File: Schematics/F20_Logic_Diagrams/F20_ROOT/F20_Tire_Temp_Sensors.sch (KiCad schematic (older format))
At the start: 6 parts

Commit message: 02/18/20 update
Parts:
- gave numbers to parts that had none: 6
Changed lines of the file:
@@
 $Descr A 11000 8500
 encoding utf-8
-Sheet 11 11
+Sheet 11 13
 Title "Tire Temperature Sensors"
 Date "2020-02-12"
@@
 $EndDescr
 $Comp
-L FSAE_Library:Tire_Temp_Sensor U?
+L FSAE_Library:Tire_Temp_Sensor U18
 U 1 1 5E3B80AD
 P 8500 1000
-F 0 "U?" H 9028 725 50  0000 L CNN
+F 0 "U18" H 9028 725 50  0000 L CNN
 F 1 "Tire_Temp_Sensor" H 8650 1050 50  0001 C CNN
 F 2 "" H 9000 1500 50  0001 C CNN
@@
 $EndComp
 $Comp
-L FSAE_Library:Tire_Temp_Sensor U?
+L FSAE_Library:Tire_Temp_Sensor U19
 U 1 1 5E3B9299
 P 8500 2000
-F 0 "U?" H 9028 1725 50  0000 L CNN
+F 0 "U19" H 9028 1725 50  0000 L CNN
 F 1 "Tire_Temp_Sensor" H 8650 2050 50  0001 C CNN
 F 2 "" H 9000 2500 50  0001 C CNN
@@
 $EndComp
 $Comp
-L FSAE_Library:Tire_Temp_Sensor U?
+L FSAE_Library:Tire_Temp_Sensor U20
 U 1 1 5E3BA080
 P 8500 3000
-F 0 "U?" H 9028 2725 50  0000 L CNN
+F 0 "U20" H 9028 2725 50  0000 L CNN
 F 1 "Tire_Temp_Sensor" H 8650 3050 50  0001 C CNN
 F 2 "" H 9000 3500 50  0001 C CNN
@@
 $EndComp
 $Comp
-L FSAE_Library:Tire_Temp_Sensor U?
+L FSAE_Library:Tire_Temp_Sensor U21
 U 1 1 5E3BAAB5
 P 8500 4000
-F 0 "U?" H 9028 3725 50  0000 L CNN
+F 0 "U21" H 9028 3725 50  0000 L CNN
 F 1 "Tire_Temp_Sensor" H 8650 4050 50  0001 C CNN
 F 2 "" H 9000 4500 50  0001 C CNN
@@
 RIM_LO_TIRE
 $Comp
-L FSAE_Library:Tire_Temp_Sensor U?
+L FSAE_Library:Tire_Temp_Sensor U22
 U 1 1 5E3CA66D
 P 8500 5000
-F 0 "U?" H 9028 4725 50  0000 L CNN
+F 0 "U22" H 9028 4725 50  0000 L CNN
 F 1 "Tire_Temp_Sensor" H 8650 5050 50  0001 C CNN
 F 2 "" H 9000 5500 50  0001 C CNN
@@
 RM
 $Comp
-L FSAE_Library:GND #PWR?
+L FSAE_Library:GND #PWR016
 U 1 1 5E3CA678
 P 4000 6950
-F 0 "#PWR?" H 4000 6750 50  0001 C CNN
+F 0 "#PWR016" H 4000 6750 50  0001 C CNN
 F 1 "GND" H 4004 6796 50  0000 C CNN
 F 2 "" H 4000 6900 50  0001 C CNN
@@
 RIM_+5V
 $Comp
-L FSAE_Library:Tire_Temp_Sensor U?
+L FSAE_Library:Tire_Temp_Sensor U23
 U 1 1 5E3CFAE2
 P 8500 6000
-F 0 "U?" H 9028 5725 50  0000 L CNN
+F 0 "U23" H 9028 5725 50  0000 L CNN
 F 1 "Tire_Temp_Sensor" H 8650 6050 50  0001 C CNN
 F 2 "" H 9000 6500 50  0001 C CNN

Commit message: 02/19/20 update
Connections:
- net RIM_LC_TIRE renamed LC_TIRE_TEMP
- net RIM_LI_TIRE renamed LI_TIRE_TEMP
- net RIM_LO_TIRE renamed LO_TIRE_TEMP
- net RIM_RI_TIRE renamed RI_TIRE_TEMP
- net RIM_RM_TIRE renamed RC_TIRE_TEMP
- net RM_RO_TIRE renamed RO_TIRE_TEMP
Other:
- note added: "LO: Left Outer\nLC: Left Center\nLI: Left Inner\nRO: Right Outer\nRC: Right Center\nRI: Right Inner\n\nAbout 2mA each\n18mA total"
- note removed: "LO: Left Outer\nLC: Left Center\nLI: Left Inner\nRO: Right Outer\nRC: Right Center\nRI: Right Inner"
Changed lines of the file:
@@
 $Descr A 11000 8500
 encoding utf-8
-Sheet 11 13
+Sheet 12 13
 Title "Tire Temperature Sensors"
 Date "2020-02-12"
@@
 Wire Wire Line
 	3500 2000 8500 2000
-Text GLabel 2500 1250 0    50   Input ~ 0
-RIM_LO_TIRE
 $Comp
 L FSAE_Library:Tire_Temp_Sensor U22
@@
 Wire Wire Line
 	3500 5000 8500 5000
-Text GLabel 2500 2250 0    50   Input ~ 0
-RIM_LC_TIRE
-Text GLabel 2500 3250 0    50   Input ~ 0
-RIM_LI_TIRE
-Text GLabel 2500 4250 0    50   Input ~ 0
-RIM_RI_TIRE
-Text GLabel 2500 5250 0    50   Input ~ 0
-RIM_RM_TIRE
-Text Notes 5550 7550 0    50   ~ 0
-LO: Left Outer\nLC: Left Center\nLI: Left Inner\nRO: Right Outer\nRC: Right Center\nRI: Right Inner
 Wire Notes Line
 	6275 7000 5500 7000
 Wire Notes Line
-	5500 7000 5500 7600
+	5500 7000 5500 7800
 Wire Notes Line
-	5500 7600 6275 7600
+	5500 7800 6275 7800
 Wire Wire Line
 	8500 6000 3500 6000
-Text GLabel 2500 6250 0    50   Input ~ 0
-RM_RO_TIRE
 Wire Wire Line
 	2500 1250 8500 1250
@@
 Wire Wire Line
 	2500 6250 8500 6250
+Text GLabel 2500 1250 0    50   Input ~ 0
+LO_TIRE_TEMP
+Text GLabel 2500 2250 0    50   Input ~ 0
+LC_TIRE_TEMP
+Text GLabel 2500 3250 0    50   Input ~ 0
+LI_TIRE_TEMP
+Text GLabel 2500 4250 0    50   Input ~ 0
+RI_TIRE_TEMP
+Text GLabel 2500 5250 0    50   Input ~ 0
+RC_TIRE_TEMP
+Text GLabel 2500 6250 0    50   Input ~ 0
+RO_TIRE_TEMP
+Text Notes 5550 7750 0    50   ~ 0
+LO: Left Outer\nLC: Left Center\nLI: Left Inner\nRO: Right Outer\nRC: Right Center\nRI: Right Inner\n\nAbout 2mA each\n18mA total
 $EndSCHEMATC

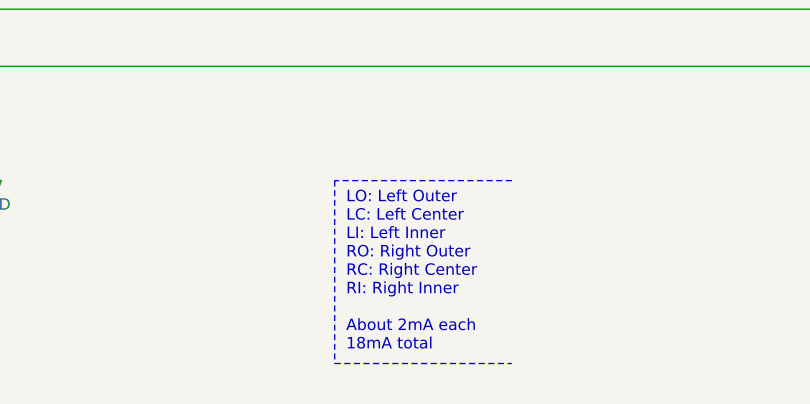
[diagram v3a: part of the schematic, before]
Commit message: Major powertrain update, added shifting schematic
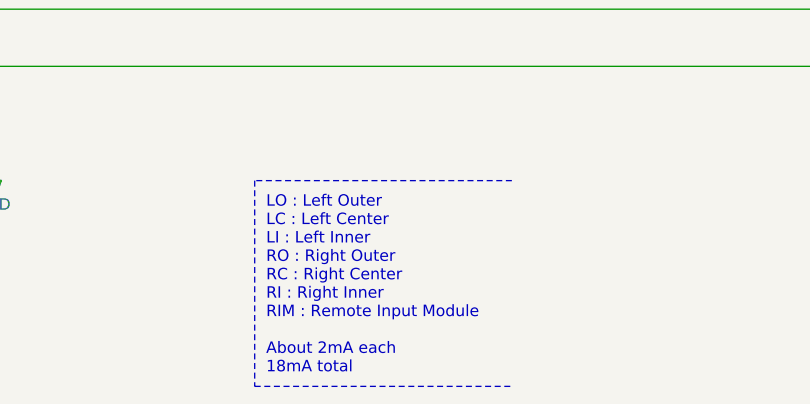
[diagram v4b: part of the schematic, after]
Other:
- note added: "LO : Left Outer\nLC : Left Center\nLI : Left Inner\nRO : Right Outer\nRC : Right Center\nRI : Right Inner\nRIM : Remote Input Module\n\nAbout 2mA each\n18mA total"
- note removed: "LO: Left Outer\nLC: Left Center\nLI: Left Inner\nRO: Right Outer\nRC: Right Center\nRI: Right Inner\n\nAbout 2mA each\n18mA total"
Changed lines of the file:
@@
 $Descr A 11000 8500
 encoding utf-8
-Sheet 12 14
+Sheet 13 15
 Title "Tire Temperature Sensors"
-Date "2020-02-12"
+Date "2020-03-03"
 Rev "A"
 Comp "F20"
@@
 	3500 5000 8500 5000
 Wire Notes Line
-	6275 7000 5500 7000
+	6275 7000 5150 7000
 Wire Notes Line
-	5500 7000 5500 7800
+	5150 7000 5150 7900
 Wire Notes Line
-	5500 7800 6275 7800
+	5150 7900 6275 7900
 Wire Wire Line
 	8500 6000 3500 6000
@@
 Text GLabel 2500 6250 0    50   Input ~ 0
 RO_TIRE_TEMP
-Text Notes 5550 7750 0    50   ~ 0
-LO: Left Outer\nLC: Left Center\nLI: Left Inner\nRO: Right Outer\nRC: Right Center\nRI: Right Inner\n\nAbout 2mA each\n18mA total
+Text Notes 5200 7850 0    50   ~ 0
+LO : Left Outer\nLC : Left Center\nLI : Left Inner\nRO : Right Outer\nRC : Right Center\nRI : Right Inner\nRIM : Remote Input Module\n\nAbout 2mA each\n18mA total
 $EndSCHEMATC

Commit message: Added steering wheel drawing, udpated some ECU pinout to match previous tune, added accel/XBEE drawing
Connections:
- net GNDPWR renamed RIM_AGND
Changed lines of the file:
@@
 EESchema Schematic File Version 4
+LIBS:F20_ROOT-cache
 EELAYER 30 0
 EELAYER END
 $Descr A 11000 8500
 encoding utf-8
-Sheet 13 15
+Sheet 13 18
 Title "Tire Temperature Sensors"
 Date "2020-03-03"
@@
 Text Notes 8850 5000 0    50   ~ 0
 RM
-$Comp
-L FSAE_Library:GND #PWR016
-U 1 1 5E3CA678
-P 4000 6950
-F 0 "#PWR016" H 4000 6750 50  0001 C CNN
-F 1 "GND" H 4004 6796 50  0000 C CNN
-F 2 "" H 4000 6900 50  0001 C CNN
-F 3 "" H 4000 6900 50  0001 C CNN
-	1    4000 6950
-	1    0    0    -1
-$EndComp
 Text GLabel 2500 1000 0    50   Input ~ 0
 RIM_+5V
@@
 Connection ~ 4000 6500
 Wire Wire Line
-	4000 6500 4000 6950
-Wire Wire Line
 	2500 6250 8500 6250
 Text GLabel 2500 1250 0    50   Input ~ 0
@@
 Text Notes 5200 7850 0    50   ~ 0
 LO : Left Outer\nLC : Left Center\nLI : Left Inner\nRO : Right Outer\nRC : Right Center\nRI : Right Inner\nRIM : Remote Input Module\n\nAbout 2mA each\n18mA total
+Text GLabel 2500 6500 0    50   Input ~ 0
+RIM_AGND
+Wire Wire Line
+	2500 6500 4000 6500
 $EndSCHEMATC
